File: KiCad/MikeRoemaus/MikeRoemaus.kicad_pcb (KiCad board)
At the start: 2 copper layers, 85 x 64 mm, 14 parts, among them J1 Conn_01x04_Socket, J2 Conn_01x04_Socket, J3 Conn_01x02_Socket, SW1 SW_DIP_x01, SW2 SW_DIP_x03

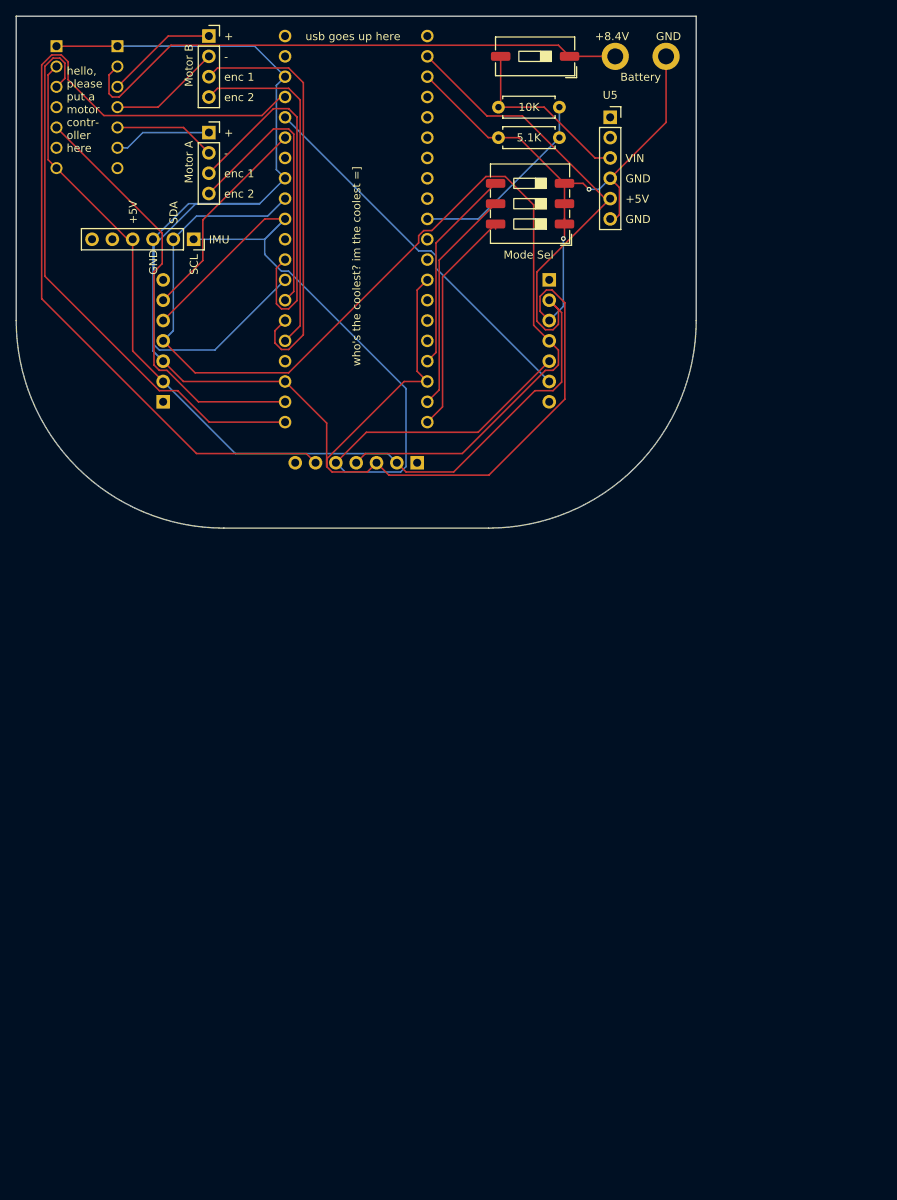
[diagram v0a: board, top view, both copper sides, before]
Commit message: resized pcb and added breakout gpio. still need to reroute and add capacitors
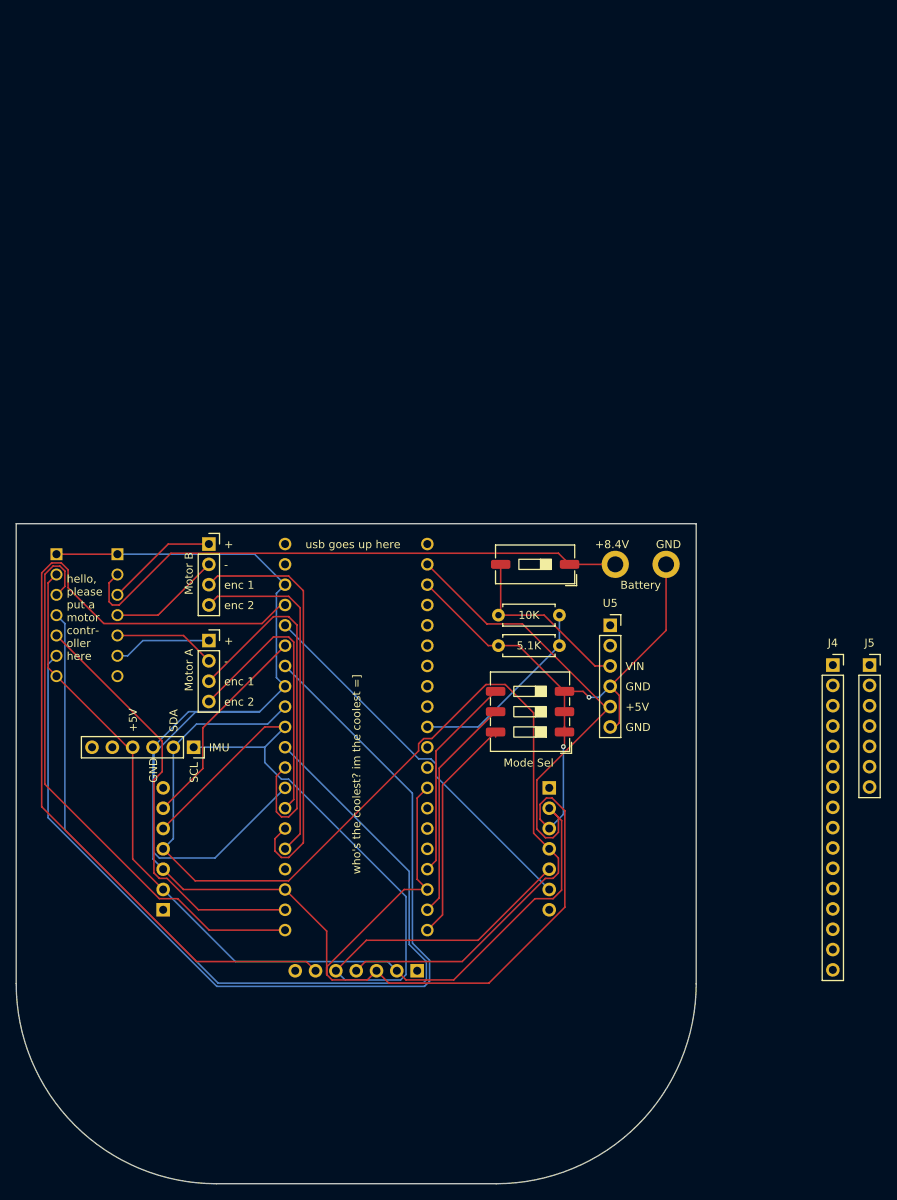
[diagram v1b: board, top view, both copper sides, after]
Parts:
- added J4: Conn_01x16_Socket, Connector_PinSocket_2.54mm:PinSocket_1x16_P2.54mm_Vertical, F.Cu at (152.3, 109.1)
- added J5: Conn_01x07_Socket, Connector_PinSocket_2.54mm:PinSocket_1x07_P2.54mm_Vertical, F.Cu at (156.9, 109.1)
- moved R1 63.5 mm to (110.5, 102.9)
- moved R2 63.5 mm to (118.1, 106.7)
- moved A2 63.5 mm to (92.7, 91.4)
- moved J1 63.5 mm to (74.3, 106.0)
- moved J2 63.5 mm to (74.3, 94.0)
- moved SW2 63.5 mm to (114.4, 114.9)
- moved U4 63.5 mm to (100.3, 147.3)
- moved U5 63.5 mm to (124.5, 104.1)
- moved U6 63.5 mm to (57.8, 90.2)
- moved J3 63.5 mm to (125.1, 96.5)
- moved SW1 63.5 mm to (115.1, 96.5)
- moved U1 63.5 mm to (72.4, 119.4)
- moved U3 63.5 mm to (116.8, 124.5)
- moved U2 63.5 mm to (68.6, 139.7)
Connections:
- A2 pad 1: unconnected-(A2-GPIO0-Pad1) -> /ToF 1
- A2 pad 10: /scl -> /motor A enc 1
- A2 pad 11: unconnected-(A2-GPIO8-Pad11) -> /motor A enc 2
- A2 pad 12: /motor A enc 1 -> /motor B enc 1
- A2 pad 14: /motor A enc 2 -> /motor B enc 2
- A2 pad 15: /motor B enc 1 -> Net-(A2-GPIO11)
- A2 pad 16: /motor B enc 2 -> /motor A pwm
- A2 pad 17: unconnected-(A2-GPIO13-Pad17) -> /motor B pwm
- A2 pad 19: /motor A pwm -> Net-(A2-GPIO14)
- A2 pad 2: unconnected-(A2-GPIO1-Pad2) -> /ToF 2
- A2 pad 20: /motor B pwm -> Net-(A2-GPIO15)
- A2 pad 25: unconnected-(A2-GPIO19-Pad25) -> Net-(A2-GPIO19)
- A2 pad 26: unconnected-(A2-GPIO20-Pad26) -> Net-(A2-GPIO20)
- A2 pad 27: unconnected-(A2-GPIO21-Pad27) -> Net-(A2-GPIO21)
- A2 pad 29: unconnected-(A2-GPIO22-Pad29) -> Net-(A2-GPIO22)
- A2 pad 4: /ToF 1 -> /ToF 3
- A2 pad 5: /ToF 2 -> /motor A selector
- A2 pad 6: /ToF 3 -> /sda
- A2 pad 7: unconnected-(A2-GPIO5-Pad7) -> /scl
- A2 pad 9: /sda -> /motor B selector
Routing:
- net /motor A selector: track 0.00 -> 124.2 mm
- net /motor B selector: track 0.00 -> 117.0 mm
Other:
- board size 85 x 64 mm -> 85 x 82.5 mm

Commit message: done with pcb (PLEASE) “Free at last, Free at last, Thank God almighty we are free at last. — Martin Luther King Jr.
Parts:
- added 10K: 10K, Resistor_THT:R_Axial_DIN0207_L6.3mm_D2.5mm_P7.62mm_Horizontal, F.Cu at (64.8, 104.1)
- added C1: C, Resistor_THT:R_Axial_DIN0207_L6.3mm_D2.5mm_P7.62mm_Horizontal, B.Cu at (78.7, 146.1)
- added C2: C, Resistor_THT:R_Axial_DIN0207_L6.3mm_D2.5mm_P7.62mm_Horizontal, B.Cu at (73.7, 104.1)
- added C3: 470uF, Capacitor_THT:CP_Axial_L11.0mm_D8.0mm_P15.00mm_Horizontal, F.Cu at (117.6, 123.8)
- added C4: 1uF, Capacitor_THT:CP_Axial_L11.0mm_D8.0mm_P15.00mm_Horizontal, F.Cu at (117.6, 132.7)
- added C5: 0.1uF, Capacitor_THT:CP_Axial_L11.0mm_D8.0mm_P15.00mm_Horizontal, B.Cu at (112.4, 145.9)
- added J6: Conn_01x02_Socket, Connector_PinSocket_2.54mm:PinSocket_1x02_P2.54mm_Vertical, F.Cu at (110.5, 111.8)
- added J7: Conn_01x02_Socket, Connector_PinSocket_2.54mm:PinSocket_1x02_P2.54mm_Vertical, F.Cu at (115.6, 111.8)
- added SW3: SW_DIP_x01, Button_Switch_THT:SW_DIP_SPSTx01_Slide_9.78x4.72mm_W7.62mm_P2.54mm, F.Cu at (64.8, 96.5)
- J1, J2: moved to B.Cu
- SW1: value SW_DIP_x01 -> SW_SPDT; footprint Button_Switch_SMD:SW_DIP_SPSTx01_Slide_9.78x4.72mm_W8.61mm_P2.54mm -> mike_lib:pwr sw
- SW2: footprint Button_Switch_SMD:SW_DIP_SPSTx03_Slide_9.78x9.8mm_W8.61mm_P2.54mm -> Button_Switch_THT:SW_DIP_SPSTx03_Slide_9.78x9.8mm_W7.62mm_P2.54mm
- moved J4 75.1 mm to (78.7, 94.0)
- moved J5 60.1 mm to (106.7, 142.2), turned to 180 degrees
- moved SW2 42.2 mm to (119.4, 156.8)
- moved J1 36.5 mm to (78.7, 142.2), turned to 90 degrees
- moved U1 34.7 mm to (86.4, 151.1), turned to 90 degrees
- moved U6 19.1 mm to (59.7, 109.2)
- moved U3 15.9 mm to (124.5, 138.4)
- moved U2 15.9 mm to (61.0, 153.7)
- moved U4 12.7 mm to (100.3, 160.0)
- moved J2 11.1 mm to (69.8, 104.1), turned to 180 degrees
- moved SW1 4.45 mm to (114.9, 92.1), turned to 0 degrees
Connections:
- A2 pad 1: /ToF 1 -> Net-(A2-GPIO0)
- A2 pad 19: Net-(A2-GPIO14) -> /sda
- A2 pad 2: /ToF 2 -> Net-(A2-GPIO1)
- A2 pad 20: Net-(A2-GPIO15) -> /scl
- A2 pad 4: /ToF 3 -> /motor A selector
- A2 pad 5: /motor A selector -> /ToF 1
- A2 pad 6: /sda -> /ToF 2
- A2 pad 7: /scl -> /ToF 3
- J3 pad 1: +7.5V -> Net-(J3-Pin_1)
- J4 pad 1: /ToF 1 -> Net-(A2-GPIO0)
- J4 pad 15: Net-(A2-GPIO14) -> /sda
- J4 pad 16: Net-(A2-GPIO15) -> /scl
- J4 pad 2: /ToF 2 -> Net-(A2-GPIO1)
- J4 pad 3: /ToF 3 -> /motor A selector
- J4 pad 4: /motor A selector -> /ToF 1
- J4 pad 5: /sda -> /ToF 2
- J4 pad 6: /scl -> /ToF 3
- R1 pad 1: Net-(U5-VIN) -> /BAT + for motors
- SW1 pad 1: +7.5V -> unconnected-(SW1-A-Pad1)
- SW1 pad 2: Net-(U5-VIN) -> Net-(J3-Pin_1)
- U5 pad 3: Net-(U5-VIN) -> /BAT + for motors
- U6 pad 13: +7.5V -> /BAT + for motors
- U6 pad 14: GND -> Net-(C3-Pad1)
- U6 pad 7: +5V -> Net-(U6-MODE)
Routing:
- net Net-(C3-Pad1): track 0.00 -> 134.9 mm, vias 0 -> 4
- net /BAT + for motors: track 0.00 -> 133.2 mm
- net +5V: track 172.4 -> 253.5 mm, vias 0 -> 1
- net /motor A selector: track 124.2 -> 49.6 mm
- net /motor B selector: track 117.0 -> 45.9 mm
- net +7.5V: track 70.5 -> 0.00 mm
- net /motor A +out: track 12.2 -> 59.5 mm
- net /ToF 1: track 108.3 -> 67.8 mm, vias 0 -> 1
- net /ToF 2: track 47.6 -> 86.0 mm, vias 0 -> 2
- net /motor A enc 2: track 35.4 -> 73.6 mm
- net /sda: track 141.1 -> 104.2 mm
- net Net-(U6-MODE): track 0.00 -> 33.9 mm
- net /motor B enc 1: track 52.5 -> 19.4 mm
- net /motor B pwm: track 70.4 -> 39.2 mm
- net /motor A -out: track 12.7 -> 43.2 mm
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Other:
- board text added: "+3.3V"
- board text added: "cap me!"
- board text added: "do me next!"
- board text added: "en"
- board text added: "in/in"
- board text added: "phew, you didnt forget about me!"

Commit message: done, but actually this time remember to thicken BAT PWR traces, and add screws
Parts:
- added H2: MountingHole, MountingHole:MountingHole_3.5mm, F.Cu at (92.7, 117.4)
- added H3: MountingHole, MountingHole:MountingHole_3.5mm, F.Cu at (110.2, 163.9)
- added H4: MountingHole, MountingHole:MountingHole_3.5mm, F.Cu at (75.2, 163.9)
- renumbered 10K to R3
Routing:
- net /BAT + for motors: track 133.2 -> 215.4 mm, vias 0 -> 4
- net GND: track 321.2 -> 328.6 mm
- net /sda: track 104.2 -> 107.6 mm
- net /scl: track 99.2 -> 101.6 mm
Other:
- board text added: "im the coolest =]"
- board text added: "who's the coolest?"
- board text removed: "who's the coolest? im the coolest =]"

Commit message: rotated imu
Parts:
- moved U1 12.7 mm to (99.1, 150.5), turned to -90 degrees
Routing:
- net /ToF 1: track 67.8 -> 78.3 mm
- net /scl: track 101.6 -> 111.3 mm, vias 0 -> 1
- net /sda: track 107.6 -> 115.4 mm
- net GND: track 328.6 -> 321.8 mm
- net +5V: track 253.5 -> 252.9 mm
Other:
- board text removed: "IMU"

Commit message: motor centered now
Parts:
- moved C1 45.5 mm to (96.5, 104.1)
- moved J1 45.5 mm to (96.5, 100.3)
- moved J2 30.7 mm to (88.9, 128.3), turned to -90 degrees
- moved C2 25.4 mm to (88.9, 124.5), turned to 0 degrees
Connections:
- C3 pad 1: Net-(C3-Pad1) -> GND
- C4 pad 1: Net-(C3-Pad1) -> GND
- C5 pad 1: Net-(C3-Pad1) -> GND
- U6 pad 14: Net-(C3-Pad1) -> GND
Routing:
- net GND: track 321.8 -> 468.6 mm, vias 2 -> 7
- net Net-(C3-Pad1): track 134.9 -> 0.00 mm, vias 4 -> 0
- net /motor A -out: track 43.2 -> 104.3 mm
- net /motor B +out: track 21.2 -> 56.6 mm
- net /motor A enc 2: track 73.6 -> 41.8 mm, vias 0 -> 1
- net /motor A enc 1: track 49.9 -> 28.0 mm, vias 0 -> 2
- net /motor B -out: track 20.5 -> 38.3 mm, vias 0 -> 1
- net /motor B enc 2: track 21.8 -> 31.1 mm, vias 0 -> 2
- net /motor A +out: track 59.5 -> 52.7 mm, vias 0 -> 2
- net /motor B enc 1: track 19.4 -> 26.2 mm
- net /ToF 1: track 78.3 -> 79.3 mm

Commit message: bhivlucu AHHHHH
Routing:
- net GND: track 468.6 -> 378.1 mm, vias 7 -> 3
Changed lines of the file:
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@@
+	)
+	(segment
+		(start 124.46 116.84)
+		(end 117.595 123.705)
+		(width 0.2)
+		(layer "F.Cu")
+		(net "GND")
 	)
 	(segment
@@
 	)
 	(segment
-		(start 84.455 146.05)
-		(end 108.52 146.05)
-		(width 0.8)
-		(layer "F.Cu")
-		(net "GND")
-	)
-	(segment
 		(start 117.24 158.985)
 		(end 119.38 156.845)
@@
 	)
 	(segment
+		(start 117.595 123.705)
+		(end 117.595 123.825)
+		(width 0.2)
+		(layer "F.Cu")
+		(net "GND")
+	)
+	(segment
 		(start 57.15 113.665)
 		(end 64.77 106.045)
@@
 	)
 	(segment
-		(start 71.12 134.62)
-		(end 73.66 137.16)
-		(width 0.8)
-		(layer "F.Cu")
-		(net "GND")
-	)
-	(segment
 		(start 57.15 114.3)
 		(end 57.15 113.665)
@@
 	)
 	(segment
-		(start 73.66 137.16)
-		(end 73.66 139.065)
-		(width 0.8)
-		(layer "F.Cu")
-		(net "GND")
-	)
-	(segment
 		(start 99.18 159.215686)
 		(end 99.18 161.19)
@@
 		(width 0.2)
 		(layer "F.Cu")
-		(net "GND")
-	)
-	(via
-		(at 84.455 146.05)
-		(size 0.6)
-		(drill 0.3)
-		(layers "F.Cu" "B.Cu")
 		(net "GND")
 	)
@@
 	)
 	(via
-		(at 108.52 146.05)
-		(size 0.6)
-		(drill 0.3)
-		(layers "F.Cu" "B.Cu")
-		(net "GND")
-	)
-	(via
 		(at 64.77 110.49)
 		(size 0.6)
 		(drill 0.3)
-		(layers "F.Cu" "B.Cu")
-		(net "GND")
-	)
-	(via
-		(at 73.66 139.065)
-		(size 0.9)
-		(drill 0.5)
 		(layers "F.Cu" "B.Cu")
 		(net "GND")
@@
 		(net "GND")
 	)
-	(via
-		(at 71.12 134.62)
-		(size 0.9)
-		(drill 0.5)
-		(layers "F.Cu" "B.Cu")
-		(net "GND")
-	)
-	(segment
-		(start 73.66 139.065)
-		(end 81.28 139.065)
-		(width 0.8)
-		(layer "B.Cu")
-		(net "GND")
-	)
-	(segment
-		(start 81.28 139.065)
-		(end 81.915 139.7)
-		(width 0.8)
-		(layer "B.Cu")
-		(net "GND")
-	)
 	(segment
 		(start 120.77 115.45)
@@
 	)
 	(segment
-		(start 55.88 112.395)
-		(end 52.705 115.57)
-		(width 0.8)
-		(layer "B.Cu")
-		(net "GND")
-	)
-	(segment
 		(start 111.055686 111.76)
 		(end 110.49 111.76)
@@
 	)
 	(segment
-		(start 62.865 112.395)
-		(end 55.88 112.395)
-		(width 0.8)
-		(layer "B.Cu")
-		(net "GND")
-	)
-	(segment
 		(start 83.82 99.06)
 		(end 82.67 100.21)
@@
 	)
 	(segment
-		(start 81.915 139.7)
-		(end 81.915 146.05)
-		(width 0.8)
-		(layer "B.Cu")
-		(net "GND")
-	)
-	(segment
 		(start 60.96 148.59)
 		(end 72.39 137.16)
@@
 	)
 	(segment
-		(start 112.275 146.05)
-		(end 112.395 145.93)
-		(width 0.8)
-		(layer "B.Cu")
-		(net "GND")
-	)
-	(segment
-		(start 52.705 115.57)
-		(end 52.705 130.81)
-		(width 0.8)
-		(layer "B.Cu")
-		(net "GND")
-	)
-	(segment
 		(start 83.82 137.16)
 		(end 91.44 144.78)
@@
 	)
 	(segment
-		(start 56.515 134.62)
-		(end 71.12 134.62)
-		(width 0.8)
-		(layer "B.Cu")
-		(net "GND")
-	)
-	(segment
 		(start 114.745686 115.45)
 		(end 111.055686 111.76)
@@
 	)
 	(segment
-		(start 81.915 146.05)
-		(end 84.455 146.05)
-		(width 0.8)
-		(layer "B.Cu")
-		(net "GND")
-	)
-	(segment
 		(start 83.82 111.76)
 		(end 85.725 113.665)
@@
 	)
 	(segment
-		(start 52.705 130.81)
-		(end 56.515 134.62)
-		(width 0.8)
-		(layer "B.Cu")
-		(net "GND")
-	)
-	(segment
-		(start 64.77 114.3)
-		(end 62.865 112.395)
-		(width 0.8)
-		(layer "B.Cu")
-		(net "GND")
-	)
-	(segment
 		(start 125.73 118.11)
 		(end 125.73 142.24)
@@
 		(layer "B.Cu")
 		(net "GND")
-	)
-	(segment
-		(start 108.52 146.05)
-		(end 112.275 146.05)
-		(width 0.8)
-		(layer "B.Cu")
-		(net "GND")
